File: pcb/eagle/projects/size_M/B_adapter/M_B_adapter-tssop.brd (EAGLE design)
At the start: 16 parts

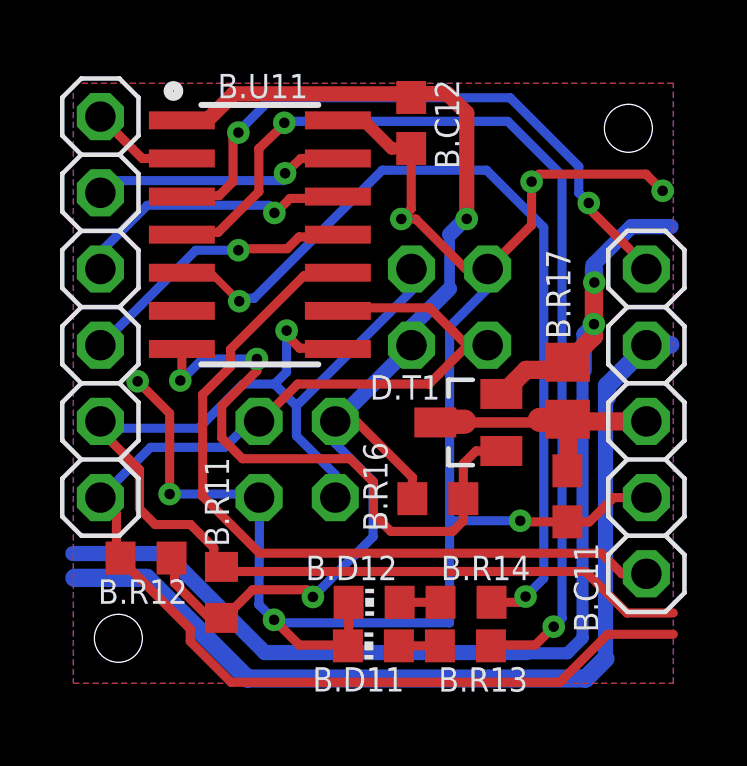
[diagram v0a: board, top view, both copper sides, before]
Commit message: changed power sleep transistor to p-channel added tssop version for attiny v2 chips
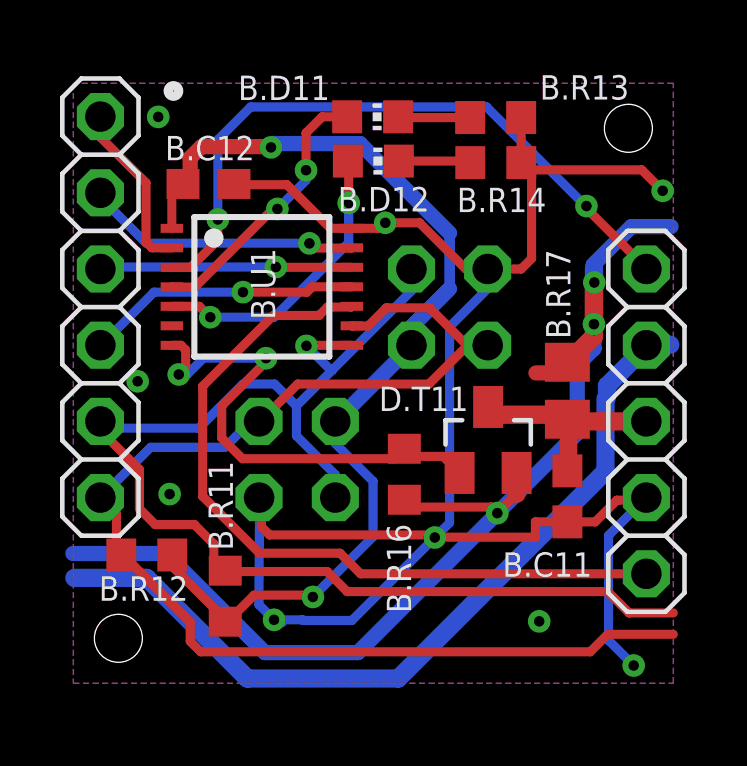
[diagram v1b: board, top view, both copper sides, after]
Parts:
- removed B.U11: AT414, atmel:SO14
- removed D.T1: FDV304, hugo:SO23
- added B.U1: ATTINY3224-XU, ATTINY412-SSN:TSSOP14
- added D.T11: FDV304, hugo:SO23
- moved B.R13 17.6 mm to (14.6, 19.4), turned to 180 degrees
- moved B.D11 17.6 mm to (10.5, 19.4), turned to 270 degrees
- moved B.D12 14.7 mm to (10.5, 17.9), turned to 270 degrees
- moved B.R14 14.7 mm to (14.6, 17.9), turned to 180 degrees
- moved B.C12 7.06 mm to (5.00, 17.1), turned to 0 degrees
- moved B.R16 1.38 mm to (11.5, 7.47), turned to 270 degrees
- moved B.R11 0.18 mm to (5.56, 3.40)
- moved B.R12 0.10 mm to (2.95, 4.78)
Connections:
- removed net N$4: B.C11.1, B.J1.3, B.R17.1, D.T1.D
- removed net PA51: B.D11.A1, B.R13.1
- new net N$1: B.D12.C1, B.R14.2
- new net N$2: B.D11.C1, B.R13.2
- net GND: now also B.R13.1, B.R14.1, B.U1.14; no longer B.D11.C1, B.D12.C1, B.U11.14
- net N$3: now also B.C11.1, B.J1.3, B.R17.1, D.T11.D; no longer B.D12.A1, B.R14.1
- net N$5: now also B.D11.A1, B.U1.4; no longer B.R13.2, B.U11.4
- net PA1: now also B.U1.11; no longer B.U11.11
- net PA2: now also B.U1.12; no longer B.U11.12
- net PA3: now also B.U1.13; no longer B.U11.13
- net PA4: now also B.U1.2; no longer B.U11.2
- net PA5: now also B.U1.3; no longer B.U11.3
- net PA7: now also B.D12.A1, B.U1.5; no longer B.R14.2, B.U11.5
- net PB2: now also B.U1.7, D.T11.G; no longer B.U11.7, D.T1.G
- net SCL: now also B.U1.9; no longer B.U11.9
- net SDA: now also B.U1.8; no longer B.U11.8
- net UPDI: now also B.U1.10; no longer B.U11.10
- net VCC: now also B.U1.1, D.T11.S; no longer B.U11.1, D.T1.S
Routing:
- net N$5: track 33.5 -> 9.12 mm
- net PA7: track 28.9 -> 9.81 mm
- net N$4: track 11.1 -> 0.00 mm
- net N$3: track 1.36 -> 8.71 mm
- net VCC: track 80.9 -> 74.6 mm, vias 4 -> 5
- net GND: track 58.4 -> 63.1 mm, vias 7 -> 9
- net PB2: track 20.5 -> 16.5 mm
- net VBAT: track 31.2 -> 27.5 mm
- net PA4: track 3.29 -> 5.75 mm
- net N$2: track 0.00 -> 2.41 mm
- net N$1: track 0.00 -> 2.40 mm
- net SDA: track 45.1 -> 43.0 mm
- net PA5: track 20.8 -> 22.3 mm
- net PA51: track 1.37 -> 0.00 mm
- net PA2: track 9.48 -> 8.41 mm
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
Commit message: version 8 main changes * ideal diode separated 3v3 DC-DC to protect it from back current * smaller package of ina 219 * usage of tssop attiny v2 in adapter * and change of PA5 to PB2 with ^ and ~ (originally used for shield power switch - now PB3) * step motor shield * out signal for BT module
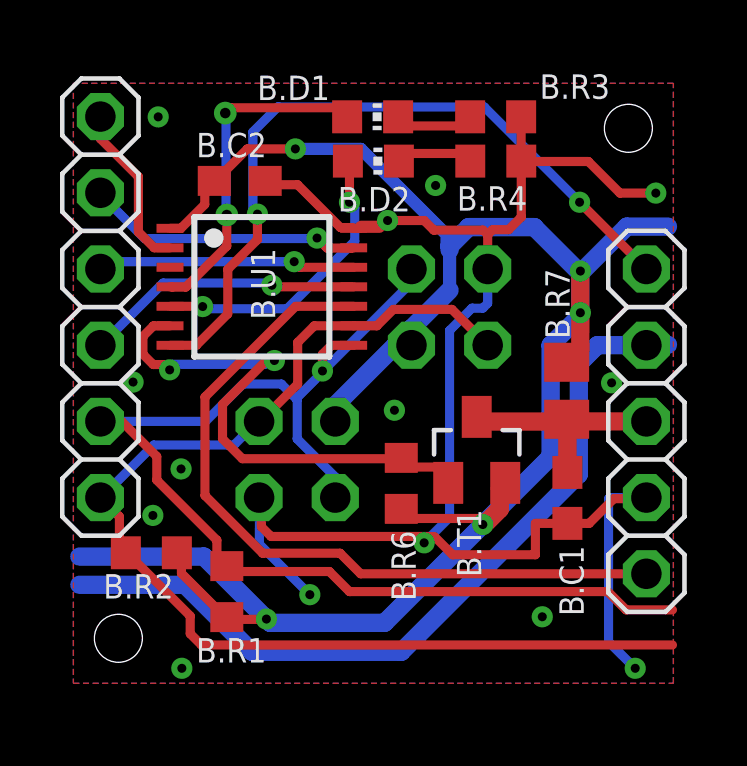
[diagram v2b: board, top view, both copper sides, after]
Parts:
- removed B.C11, B.C12: 100n, rcl:C0603
- removed B.R11, B.R12, B.R14: 2k2, rcl:R0603
- removed B.R13: 330, rcl:R0603
- removed B.R16: 100k, rcl:R0603
- removed B.R17: alt fuse or 0R, hugo:FUSE
- removed D.T11: FDV304, hugo:SO23
- added B.C1, B.C2: 100n, rcl:C0603
- added B.R1, B.R2, B.R4: 2k2, rcl:R0603
- added B.R3: 330, rcl:R0603
- added B.R6: 100k, rcl:R0603
- added B.R7: alt fuse or 0R, hugo:FUSE
- added B.T1: FDV304, hugo:SO23
- renumbered B.D11 to B.D1, B.D12 to B.D2
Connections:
- removed net PA5: B.J1.1, B.U1.3
- new net PB3: B.R6.1, B.T1.G, B.U1.6
- net GND: now also B.C1.2, B.C2.2, B.R3.1, B.R4.1; no longer B.C11.2, B.C12.2, B.R13.1, B.R14.1
- net N$1: now also B.R4.2; no longer B.R14.2
- net N$2: now also B.R3.2; no longer B.R13.2
- net N$3: now also B.C1.1, B.R7.1, B.T1.D; no longer B.C11.1, B.R17.1, D.T11.D
- net PB2: now also B.J1.1; no longer B.R16.1, D.T11.G
- net SCL: now also B.R2.1; no longer B.R12.1
- net SDA: now also B.R1.1; no longer B.R11.1
- net VCC: now also B.C2.1, B.R1.2, B.R2.2, B.R6.2, B.R7.2, B.T1.S; no longer B.C12.1, B.R11.2, B.R12.2, B.R16.2, B.R17.2, D.T11.S
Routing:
- net PA5: track 22.3 -> 0.00 mm, vias 2 -> 0
- net PB3: track 0.00 -> 18.1 mm, vias 0 -> 2
- net PB2: track 16.5 -> 24.7 mm
- net VCC: track 74.6 -> 67.1 mm
- net GND: track 63.1 -> 57.0 mm, vias 9 -> 14
- net SCL: track 43.2 -> 39.3 mm
- net N$5: track 9.12 -> 11.2 mm
- net SDA: track 43.0 -> 41.3 mm
- net N$3: track 8.71 -> 7.64 mm
- net VBAT: track 27.5 -> 27.0 mm
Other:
- board text added: "PB2 ^~"
- board text added: "adapter TSSOP M8"
- board text removed: "PA5 VREF ~"
- board text removed: "adapter M8"

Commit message: PCB v9
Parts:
- removed B.J1: (no value), pinhead2:1X05
- added B.J5: (no value), pinhead2:1X06
- moved B.R1 2.96 mm to (3.84, 5.92)
- moved B.R2 2.93 mm to (5.59, 3.30)
- moved B.R4 0.62 mm to (14.7, 17.3)
- moved B.R3 0.13 mm to (14.7, 19.3)
- moved B.R6 0.13 mm to (11.4, 7.29)
- moved B.D2 0.10 mm to (10.5, 17.8)
- moved B.D1 0.06 mm to (10.5, 19.3)
- moved B.C2 0.06 mm to (6.10, 17.2)
- moved B.T1 0.05 mm to (13.9, 8.33)
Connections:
- new net PA6: B.J5.1, B.U1.4
- net GND: now also B.J5.4; no longer B.J1.4
- net N$3: now also B.J5.3; no longer B.J1.3
- net N$5: now also B.U1.3; no longer B.U1.4
- net PB2: now also B.J5.6; no longer B.J1.1
- net UPDI: now also B.J5.5; no longer B.J1.5
- net VBAT: now also B.J5.2; no longer B.J1.2
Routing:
- net PA6: track 0.00 -> 22.9 mm, vias 0 -> 2
- net GND: track 57.0 -> 46.2 mm, vias 14 -> 18
- net SDA: track 41.3 -> 35.4 mm
- net PB3: track 18.1 -> 16.0 mm
- net PB2: track 24.7 -> 23.8 mm, vias 2 -> 1
- net VBAT: track 27.0 -> 26.1 mm
- net N$5: track 11.2 -> 10.6 mm
- net VCC: track 67.1 -> 67.6 mm
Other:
- board text added: "D6"
- board text added: "PA6 ^ DAC"
- board text added: "adapter M9.2"
- board text removed: "adapter TSSOP M8"
